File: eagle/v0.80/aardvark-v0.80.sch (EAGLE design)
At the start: 28 parts, among them IC1 LM1117-3.3, J1 USB_MINI-B_SMT, U1 CH340C

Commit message: updated v0.80 w reset, boot, second schematic sheet
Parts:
- added C5: 100nF, rcl:C-USC0805
- added Q1, Q2: TRANS_NPN-MMBT2222AL, SparkFun-DiscreteSemi:TRANS_NPN-MMBT2222AL
- added R3, R4: 10k, rcl:R-US_R0805
- added S2: BOOT, SparkFun-Switches:MOMENTARY-SWITCH-SPST-SMD-6.0X3.5MM
- C3: value 4.7uF -> 100nF
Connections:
- new net !DTR: Q2.E, R3.2, U1.!DTR
- new net !RTS: Q1.E, R4.2, U1.!RTS
- new net N$10: Q1.B, R3.1
- new net N$11: Q2.B, R4.1
- net EN: now also Q1.C; no longer U1.!RTS
- net GND: now also C5.2, S2.1
- net GP9: now also C5.1, Q2.C, S2.2; no longer U1.!DTR
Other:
- note added: "Additional Features"
- note added: "DRAFT"
- note added: "Note: See schematic sheet two for additional circuitry."
- note added: "RESET, BOOT"
- note added: "See Sheet One"
- note added: "Triangle Embedded Users Group (TriEmbed) CC BY-SA 2.0"
- note added: "Your ideas go here"
- note added: "https://github.com/TriEmbed/aardvark"
- note removed: "Note: Additional schematic sheets are available. What's on this sheet will probably be declared "the core" and pushed to another sheet to make room for custom circuitry here."

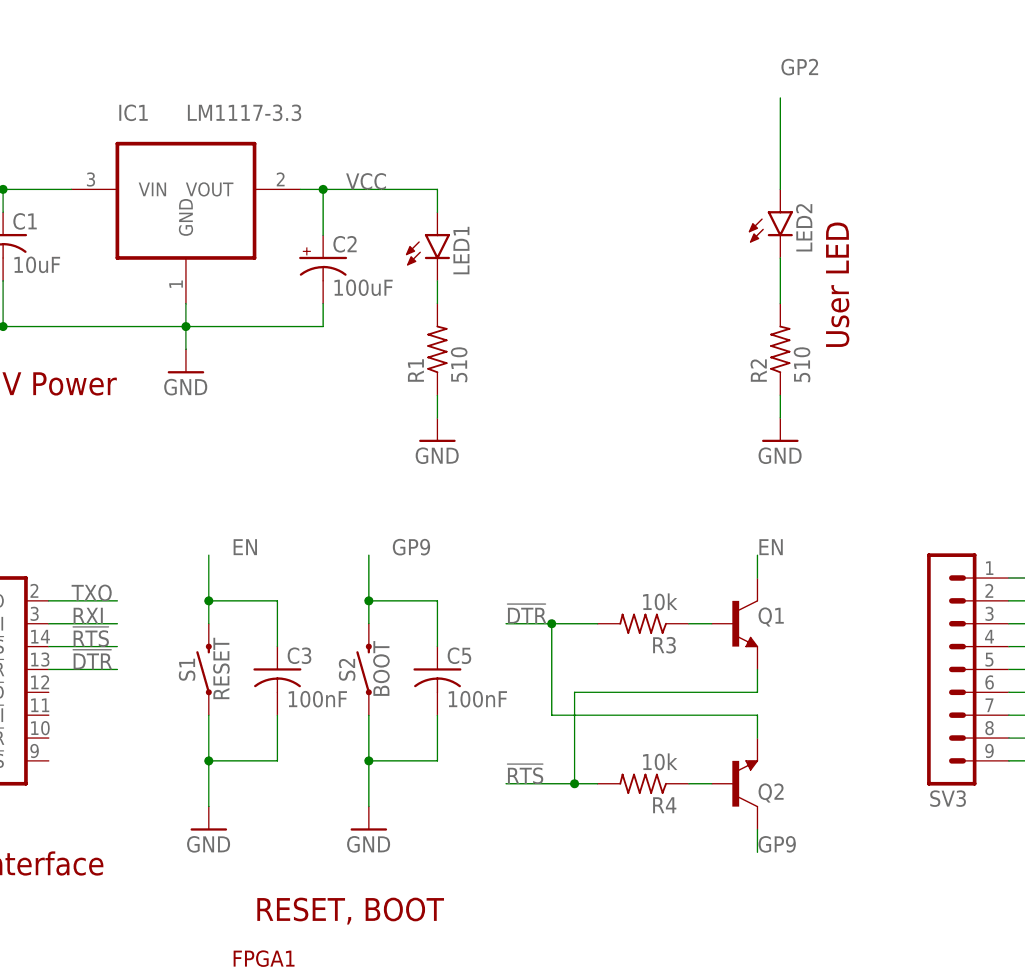
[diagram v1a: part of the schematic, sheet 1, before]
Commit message: proper momentary and power switches for v0.80
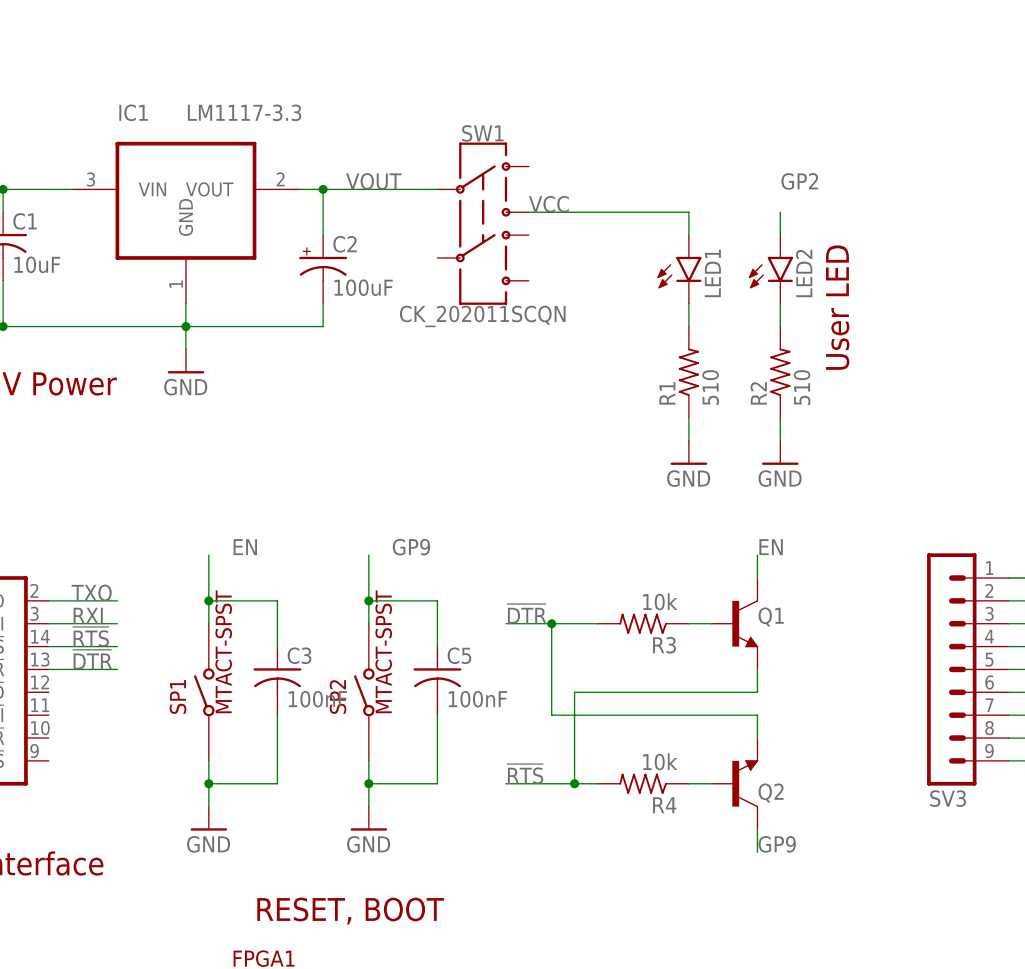
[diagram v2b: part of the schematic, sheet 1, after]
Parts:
- removed S1: RESET, SparkFun-Switches:MOMENTARY-SWITCH-SPST-SMD-6.0X3.5MM
- removed S2: BOOT, SparkFun-Switches:MOMENTARY-SWITCH-SPST-SMD-6.0X3.5MM
- added SP1, SP2: MTACT-SPST, CK-ATS2D1G_NC_LFS:MTACT-SPST
- added SW1: CK_202011SCQN, CK_JS202011SCQN:CK_202011SCQN
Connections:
- new net VOUT: C2.+, IC1.VOUT, SW1.C1
- net EN: now also SP1.PIN2; no longer S1.2
- net GND: now also SP1.PIN1, SP2.PIN1; no longer S1.1, S2.1
- net GP9: now also SP2.PIN2; no longer S2.2
- net VCC: now also SW1.1-NO; no longer C2.+, IC1.VOUT
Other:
- moved on the sheet: LED1, LED2, R1, R2
